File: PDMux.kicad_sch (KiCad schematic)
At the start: 3 parts, among them U7 74HCT4051

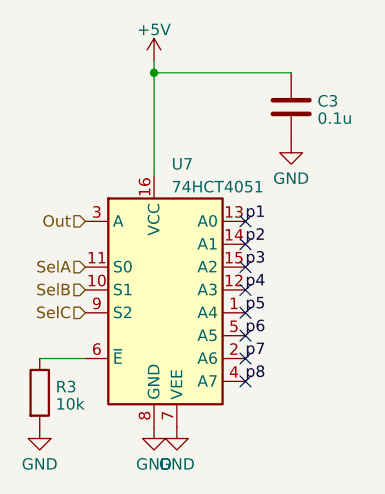
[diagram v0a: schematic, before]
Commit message: Added photodiode connector, haven't routed
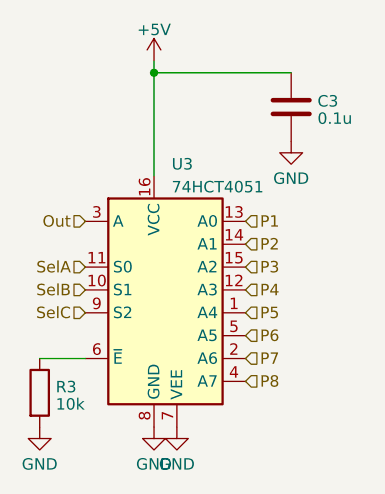
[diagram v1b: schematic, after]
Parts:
- renumbered U7 to U3
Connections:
- net p1 renamed P1
- net p2 renamed P2
- net p3 renamed P3
- net p4 renamed P4
- net p5 renamed P5
- net p6 renamed P6
- net p7 renamed P7
- net p8 renamed P8
- no-connect marks 8 -> 0
